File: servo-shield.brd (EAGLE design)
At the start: 65 x 56 mm, 34 parts, among them K1 PIN20X2

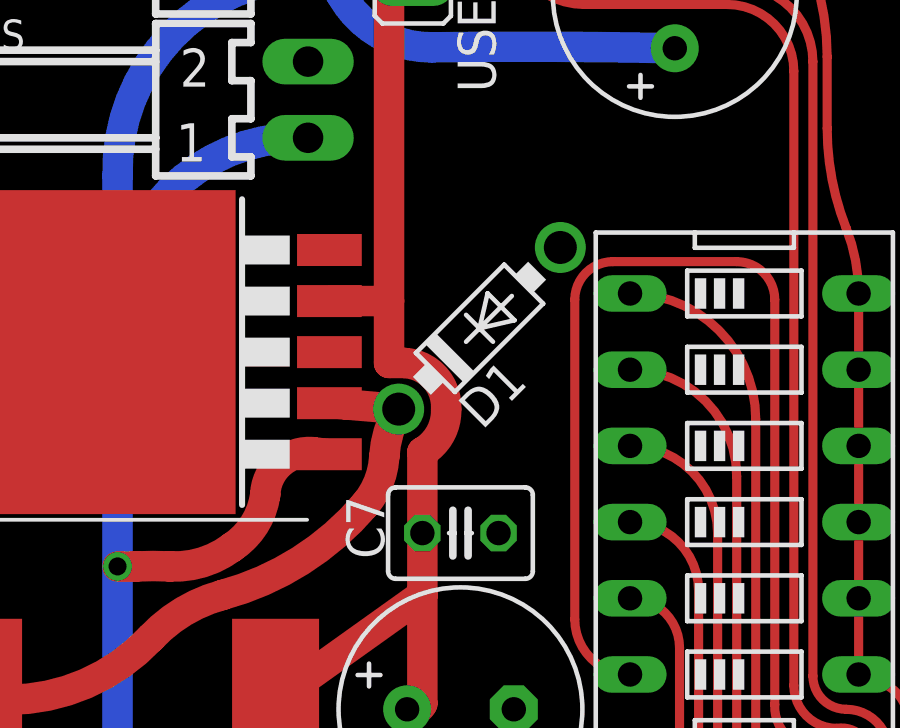
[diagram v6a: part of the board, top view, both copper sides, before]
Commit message: Rotated D1 a bit to clear the DIP grid better.
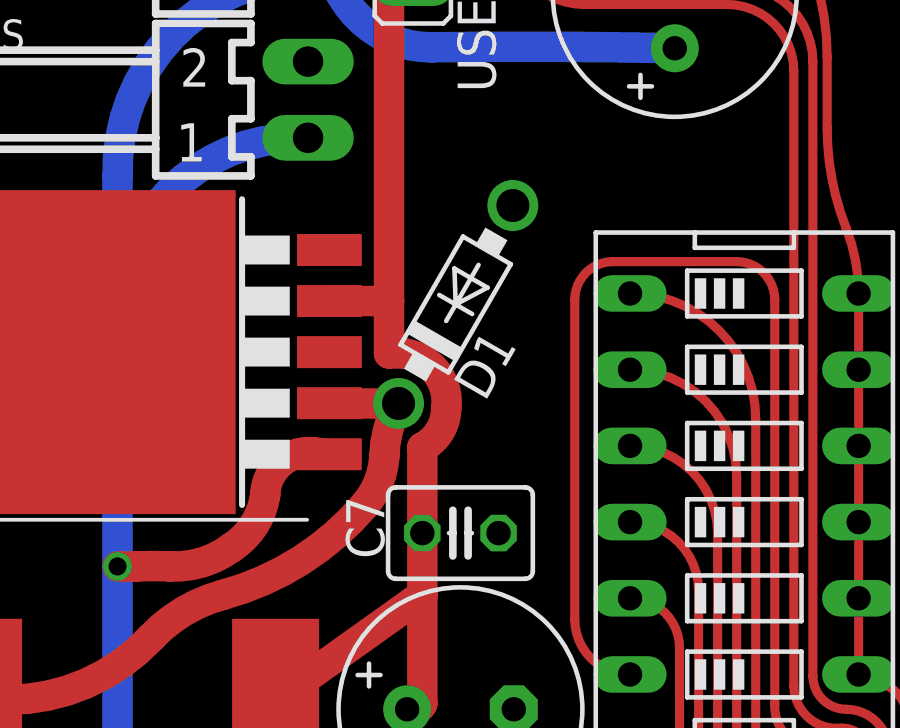
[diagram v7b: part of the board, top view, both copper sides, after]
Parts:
- moved D1 1.12 mm to (18.3, 34.4), turned to 60 degrees
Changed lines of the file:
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@@
 <attribute name="VALUE" x="13.843" y="39.71925" size="1.27" layer="27" rot="R180"/>
 </element>
-<element name="D1" library="diode" package="DO41-7.6" value="1N5824" x="19.05" y="33.655" smashed="yes" rot="R45">
-<attribute name="NAME" x="19.1398" y="30.242496875" size="1.27" layer="25" ratio="10" rot="R45"/>
-<attribute name="VALUE" x="19.67861875" y="30.152696875" size="1.27" layer="27" ratio="10" rot="R45"/>
+<element name="D1" library="diode" package="DO41-7.6" value="1N5824" x="18.25625" y="34.44875" smashed="yes" rot="R60">
+<attribute name="NAME" x="19.226209375" y="31.175765625" size="1.27" layer="25" ratio="10" rot="R60"/>
+<attribute name="VALUE" x="19.769909375" y="31.22848125" size="1.27" layer="27" ratio="10" rot="R60"/>
 </element>
 <element name="L1" library="WE-PD" package="WE-PD_1260/1245/1280/1210" value="33uh" x="7.3025" y="21.2725" smashed="yes">
@@
 <wire x1="17.145" y1="24.765" x2="17.145" y2="26.82875" width="1.016" layer="1"/>
 <wire x1="12.2525" y1="21.2725" x2="17.145" y2="24.765" width="1.016" layer="1"/>
-<wire x1="16.03375" y1="34.56305" x2="16.03375" y2="32.4993" width="1.016" layer="1"/>
-<wire x1="16.03375" y1="32.4993" x2="16.55445" y2="32.4993" width="1.016" layer="1"/>
-<wire x1="16.55445" y1="32.4993" x2="17.93875" y2="30.95625" width="1.016" layer="1" curve="-90"/>
-<wire x1="17.93875" y1="30.95625" x2="17.145" y2="29.5275" width="1.016" layer="1" curve="-61.927542"/>
-<wire x1="17.145" y1="29.5275" x2="17.145" y2="26.82875" width="1.016" layer="1"/>
+<wire x1="16.03375" y1="34.56305" x2="16.03375" y2="32.8168" width="1.016" layer="1"/>
+<wire x1="16.03375" y1="32.8168" x2="16.55445" y2="32.8168" width="1.016" layer="1"/>
+<wire x1="16.55445" y1="32.8168" x2="17.93875" y2="30.95625" width="1.016" layer="1" curve="-90"/>
+<wire x1="17.93875" y1="30.95625" x2="17.145" y2="29.68625" width="1.016" layer="1" curve="-61.927542"/>
+<wire x1="17.145" y1="29.68625" x2="17.145" y2="26.82875" width="1.016" layer="1"/>
 <contactref element="USE_REG" pad="1"/>
 <wire x1="14.0462" y1="34.56305" x2="16.03375" y2="34.56305" width="1.016" layer="1"/>
@@
 <wire x1="10.4775" y1="24.765" x2="15.24" y2="27.78125" width="1.016" layer="1" curve="34.554646"/>
 <wire x1="15.24" y1="27.78125" x2="15.875" y2="29.36875" width="1.016" layer="1" curve="37.147686"/>
-<wire x1="15.875" y1="29.36875" x2="16.355921875" y2="30.960921875" width="1.016" layer="1" curve="-27.159354"/>
-<wire x1="14.0462" y1="31.15945" x2="14.605" y2="31.115" width="1.016" layer="1"/>
-<wire x1="14.605" y1="31.115" x2="16.355921875" y2="30.960921875" width="1.016" layer="1" curve="-0.961869"/>
+<wire x1="15.875" y1="29.36875" x2="16.35125" y2="31.149190625" width="1.016" layer="1" curve="-27.159354"/>
+<wire x1="16.35125" y1="31.149190625" x2="14.0462" y2="31.149190625" width="1.016" layer="1"/>
+<wire x1="14.0462" y1="31.149190625" x2="14.0462" y2="31.15945" width="1.016" layer="1"/>
 </signal>
 <signal name="N$4">

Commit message: Rearranged C3 & C5 to be more pleasingly symmetrical
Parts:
- moved C5 5.50 mm to (54.0, 11.9), turned to 90 degrees
- moved C3 5.24 mm to (59.8, 10.8), turned to 90 degrees
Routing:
- net V+: track 141.9 -> 143.7 mm
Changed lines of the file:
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@@
 <attribute name="VALUE" x="16.129" y="17.907" size="1.27" layer="27" ratio="10"/>
 </element>
-<element name="C3" library="rcl" package="E3,5-8" value="1000uf" x="55.5625" y="13.81125" smashed="yes" rot="R180">
-<attribute name="NAME" x="58.8645" y="10.25525" size="1.27" layer="25" ratio="10"/>
-<attribute name="VALUE" x="57.8485" y="16.85925" size="1.27" layer="27" ratio="10" rot="R180"/>
-</element>
-<element name="C5" library="rcl" package="C025-030X050" value="100nf" x="57.785" y="7.9375" smashed="yes" rot="R180">
-<attribute name="NAME" x="60.42025" y="7.9375" size="1.27" layer="25" ratio="10"/>
-<attribute name="VALUE" x="60.071" y="10.9855" size="1.27" layer="27" ratio="10" rot="R180"/>
+<element name="C3" library="rcl" package="E3,5-8" value="1000uf" x="59.84875" y="10.795" smashed="yes" rot="R90">
+<attribute name="NAME" x="56.007" y="5.81025" size="1.27" layer="25" ratio="10"/>
+<attribute name="VALUE" x="62.89675" y="8.509" size="1.27" layer="27" ratio="10" rot="R90"/>
+</element>
+<element name="C5" library="rcl" package="C025-030X050" value="100nf" x="53.975" y="11.90625" smashed="yes" rot="R90">
+<attribute name="NAME" x="51.97475" y="14.44625" size="1.27" layer="25" ratio="10" rot="R180"/>
+<attribute name="VALUE" x="57.023" y="9.62025" size="1.27" layer="27" ratio="10" rot="R90"/>
 </element>
 <element name="C7" library="rcl" package="C025-030X050" value="100nf" x="18.415" y="26.82875" smashed="yes">
@@
 <contactref element="C5" pad="1"/>
 <contactref element="PWR" pad="1"/>
-<wire x1="57.3405" y1="13.81125" x2="57.3405" y2="9.652" width="1.016" layer="1"/>
-<wire x1="57.3405" y1="9.652" x2="59.055" y2="7.9375" width="1.016" layer="1"/>
-<wire x1="53.34" y1="4.953" x2="56.0705" y2="4.953" width="1.016" layer="1"/>
-<wire x1="56.0705" y1="4.953" x2="59.055" y2="7.9375" width="1.016" layer="1"/>
 <wire x1="53.34" y1="4.953" x2="51.054" y2="4.953" width="1.016" layer="1"/>
 <wire x1="51.054" y1="4.953" x2="50.8" y2="5.207" width="1.016" layer="1"/>
@@
 <wire x1="14.44625" y1="44.7675" x2="17.4625" y2="43.02125" width="1.016" layer="16" curve="61.636686"/>
 <wire x1="17.4625" y1="43.02125" x2="25.55875" y2="42.9895" width="1.016" layer="16" curve="-1.948885"/>
+<wire x1="53.34" y1="4.953" x2="55.78475" y2="4.953" width="1.016" layer="1"/>
+<wire x1="55.78475" y1="4.953" x2="59.84875" y2="9.017" width="1.016" layer="1" curve="90"/>
+<wire x1="53.34" y1="4.953" x2="55.40375" y2="7.01675" width="1.016" layer="1" curve="90"/>
+<wire x1="53.975" y1="10.63625" x2="55.40375" y2="9.2075" width="1.016" layer="1" curve="-90"/>
+<wire x1="55.40375" y1="9.2075" x2="55.40375" y2="7.01675" width="1.016" layer="1"/>
 </signal>
 <signal name="VOUT">
